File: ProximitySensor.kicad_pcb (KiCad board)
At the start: 2 copper layers, 45 x 17 mm, 17 parts, among them Q1 Q_PMOS_GSD, Q2 Q_NMOS_GSD, U1 L78L05_SOT89, U2 LM393, X1 CONN_3

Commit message: New topology
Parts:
- added J1: Conn_01x02_Male, Pin_Headers:Pin_Header_Straight_1x02_Pitch2.54mm, F.Cu at (157.2, 111.7)
- added J2: Conn_01x03_Male, Pin_Headers:Pin_Header_Straight_1x03_Pitch2.54mm, F.Cu at (150.9, 113.7)
- added J3: Conn_01x02_Male, Pin_Headers:Pin_Header_Straight_1x02_Pitch2.54mm, F.Cu at (148.4, 102.7)
- added R10: 5k, Resistors_SMD:R_0805_HandSoldering, B.Cu at (126.4, 108.4)
- added R11: 470R, Resistors_SMD:R_0805_HandSoldering, B.Cu at (148.2, 104.8)
- added R6: 5k, Resistors_SMD:R_0805_HandSoldering, B.Cu at (148.6, 108.4)
- added R7: 5k, Resistors_SMD:R_0805_HandSoldering, B.Cu at (151.4, 103.4)
- added R8: 5k, Resistors_SMD:R_0805_HandSoldering, B.Cu at (153.6, 113.1)
- added R9: 100R, Resistors_SMD:R_0805_HandSoldering, B.Cu at (132.0, 113.5)
- added REF**: MountingHole_2.5mm, Mounting_Holes:MountingHole_2.5mm, F.Cu at (144.9, 108.1)
- added X2: CONN_3, Connectors_Terminal_Blocks:TerminalBlock_Philmore_TB133_03x5mm_Straight, F.Cu at (165.3, 103.0)
- C3: value C -> 100nF
- D1: value LED_ALT -> D_Zener; footprint LEDs:LED_D1.8mm_W3.3mm_H2.4mm -> Capacitors_SMD:C_0805_HandSoldering; moved to B.Cu
- D2: value LED_ALT -> LED_POWER; footprint LEDs:LED_D1.8mm_W1.8mm_H2.4mm_Horizontal_O1.27mm_Z8.2mm -> LEDs:LED_D1.8mm_W3.3mm_H2.4mm
- D3: value BP104 -> LED_SIGNAL; footprint LEDs:LED_D1.8mm_W1.8mm_H2.4mm_Horizontal_O1.27mm_Z8.2mm -> LEDs:LED_D1.8mm_W3.3mm_H2.4mm
- R1: value 470R -> 100k
- R4: value R -> 5k
- R5: value R -> 470R
- moved D2 18.3 mm to (142.5, 101.7), turned to 270 degrees
- moved D3 18.1 mm to (142.5, 111.9), turned to 270 degrees
- moved D1 16.9 mm to (132.3, 105.5)
- moved R2 16.0 mm to (141.2, 108.2), turned to 90 degrees
- moved R1 12.6 mm to (133.2, 102.2), turned to 0 degrees
- moved R5 12.0 mm to (140.3, 113.4)
- moved C2 9.86 mm to (138.0, 112.2), turned to 270 degrees
- moved U2 6.90 mm to (156.7, 106.6), turned to 270 degrees
- moved R4 5.83 mm to (150.3, 108.4), turned to 270 degrees
- moved RV1 4.81 mm to (136.6, 109.8), turned to 180 degrees
- moved C3 4.39 mm to (129.7, 109.3), turned to 90 degrees
- moved R3 2.86 mm to (152.2, 108.4)
- moved C1 2.30 mm to (134.4, 105.5)
- moved U1 1.39 mm to (138.2, 105.2)
- moved Q1 1.20 mm to (128.2, 103.4)
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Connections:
- C1 pad 1: Net-(C1-Pad1) -> /Vcc
- D1 pad 1: /Gnd -> /Vcc
- D3 pad 1: /Gnd -> Net-(D3-Pad1)
- Q1 pad 1: /Gnd -> Net-(D1-Pad2)
- Q1 pad 2: Net-(C1-Pad1) -> /Vcc
- R1 pad 1: /5v -> Net-(D1-Pad2)
- R1 pad 2: Net-(D1-Pad2) -> /Gnd
- R3 pad 2: Net-(D3-Pad2) -> Net-(J1-Pad2)
- R4 pad 1: Net-(Q2-Pad1) -> /5v
- R4 pad 2: /5v -> Net-(D3-Pad1)
- R5 pad 1: Net-(C1-Pad1) -> /5v
- R5 pad 2: Net-(Q2-Pad3) -> Net-(D3-Pad2)
- U1 pad 3: Net-(C1-Pad1) -> /Vcc
- U2 pad 1: Net-(Q2-Pad1) -> Net-(J2-Pad1)
- U2 pad 2: Net-(U2-Pad2) -> Net-(D3-Pad1)
- U2 pad 3: Net-(D3-Pad2) -> Net-(R6-Pad2)
- U2 pad 5: (no net) -> /sign
- U2 pad 6: (no net) -> Net-(C3-Pad1)
- U2 pad 7: (no net) -> Net-(D3-Pad1)
- U2 pad 8: Net-(C1-Pad1) -> /Vcc
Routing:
- net Net-(C3-Pad1): track 3.54 -> 49.4 mm, vias 0 -> 2
- net /Vcc: track 0.00 -> 40.4 mm, vias 0 -> 2
- net Net-(C1-Pad1): track 35.2 -> 0.00 mm
- net Net-(Q2-Pad1): track 31.2 -> 2.42 mm, vias 2 -> 0
- net Net-(D3-Pad1): track 0.00 -> 25.1 mm, vias 0 -> 2
- net Net-(J2-Pad2): track 0.00 -> 23.6 mm
- net Net-(J3-Pad1): track 0.00 -> 21.0 mm
- net Net-(R6-Pad2): track 0.00 -> 19.1 mm
- net Net-(J2-Pad1): track 0.00 -> 17.7 mm, vias 0 -> 2
- net /Gnd: track 101.6 -> 118.8 mm
- net /sign: track 0.00 -> 11.3 mm
- net Net-(J1-Pad2): track 0.00 -> 8.47 mm
- net Net-(D3-Pad2): track 9.02 -> 2.47 mm
- net /5v: track 31.8 -> 38.3 mm
- net Net-(D1-Pad2): track 3.54 -> 5.23 mm
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- added copper zone on B.Cu, net /Gnd
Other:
- board size 45 x 17 mm -> 53.1 x 16.7 mm
- net class small added: clearance 0.25, trace_width 0.3, via_dia 0.6, via_drill 0.4

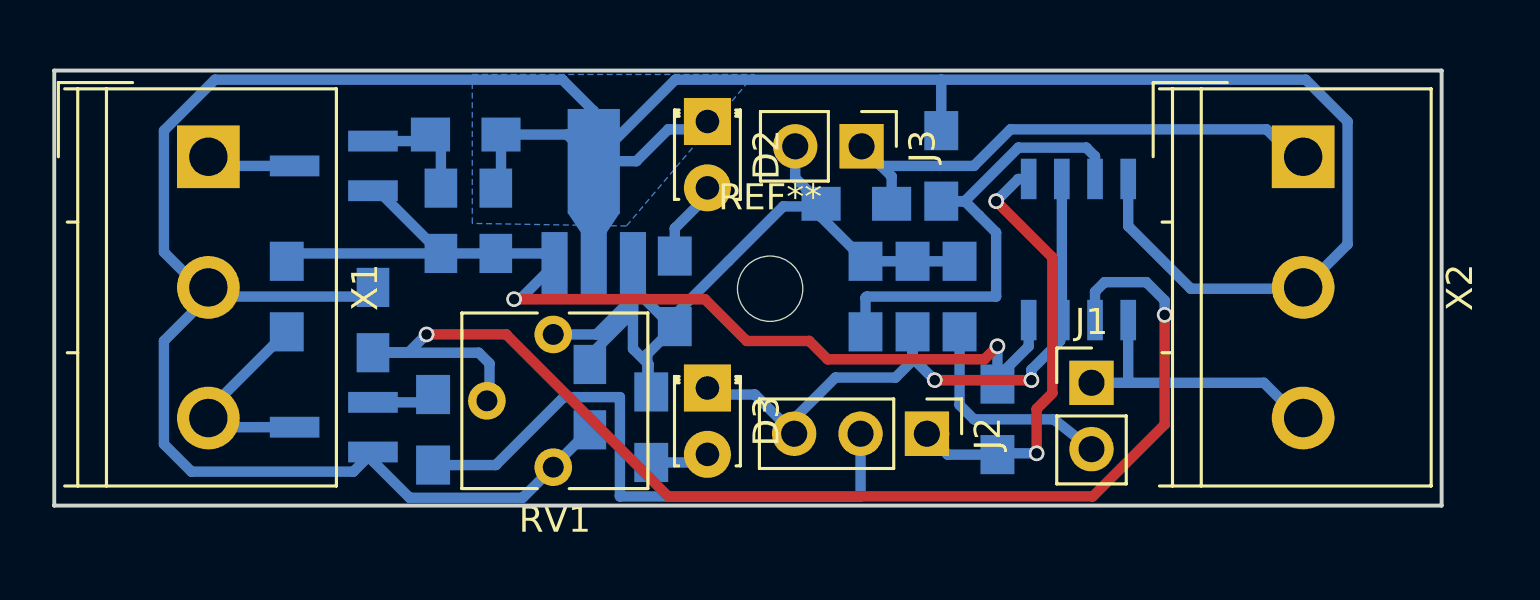
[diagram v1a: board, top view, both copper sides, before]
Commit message: add D_Zener
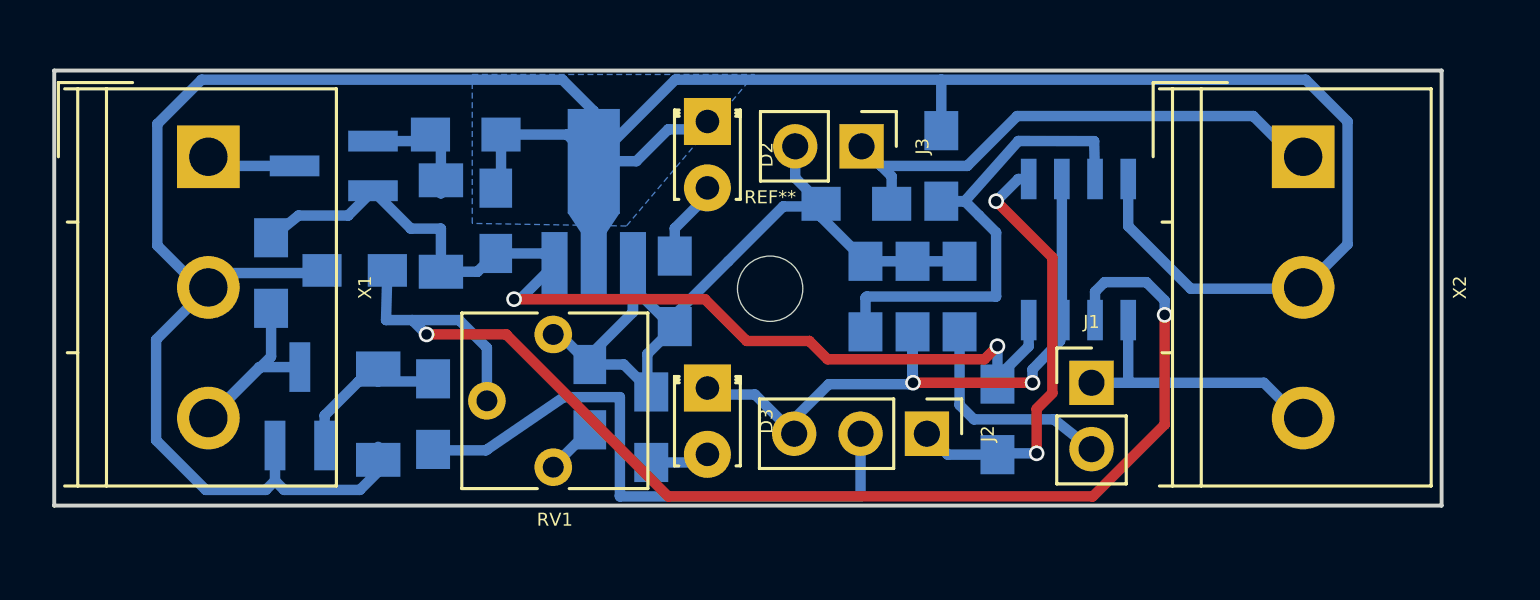
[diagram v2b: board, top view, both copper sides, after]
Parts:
- added D4: D_Zener, Diodes_SMD:D_MiniMELF, B.Cu at (129.9, 112.9)
- D1: footprint Capacitors_SMD:C_0805_HandSoldering -> Diodes_SMD:D_MiniMELF
- moved C3 2.02 mm to (129.0, 107.4), turned to 180 degrees
- moved Q2 1.53 mm to (126.9, 112.6), turned to 90 degrees
- moved R10 1.08 mm to (125.8, 107.5)
- moved R9 0.60 mm to (132.0, 112.9)
- moved D1 0.20 mm to (132.3, 105.7)
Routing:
- net /Gnd: track 118.8 -> 112.9 mm
- net /5v: track 38.3 -> 33.0 mm
- net Net-(D4-Pad1): track 2.42 -> 6.02 mm
- net Net-(Q2-Pad3): track 8.19 -> 9.73 mm
- net Net-(D3-Pad1): track 25.1 -> 26.3 mm
- net Net-(J2-Pad1): track 17.7 -> 16.9 mm
- net /Vcc: track 40.4 -> 41.1 mm
- net Net-(R6-Pad2): track 19.1 -> 19.7 mm
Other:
- rule trace_min: 0.2 -> 0.3
- rule via_min_size: 0.4 -> 0.5

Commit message: add some small changes
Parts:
- added REF**: MountingHole_5mm, Mounting_Holes:MountingHole_5mm, F.Cu at (144.9, 108.1)
- C3: value 100nF -> 0,1uF
- R10, R4, R6, R7, R8: value 5k -> 10K
- R11, R2, R5: value 470R -> 1K
- R3: value 10k -> 10K
- moved R4 3.38 mm to (148.8, 111.4), turned to 180 degrees
- moved R2 0.55 mm to (140.7, 108.2)
- moved U1 0.55 mm to (137.6, 105.2)
- moved R3 0.30 mm to (152.1, 108.1)
- moved R6 0.30 mm to (148.6, 108.1)
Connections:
- R4 pad 1: /5v -> /Vcc
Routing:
- net /Vcc: track 41.1 -> 56.3 mm, vias 2 -> 4
- net /5v: track 33.0 -> 34.2 mm
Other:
- rule trace_min: 0.3 -> 0.25
- board text added: "J1"
- board text added: "J2"
- board text added: "J3"
- board text added: "Proximity Sensor 1.0"
